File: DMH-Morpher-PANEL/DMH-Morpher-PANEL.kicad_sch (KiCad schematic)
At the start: 4 parts

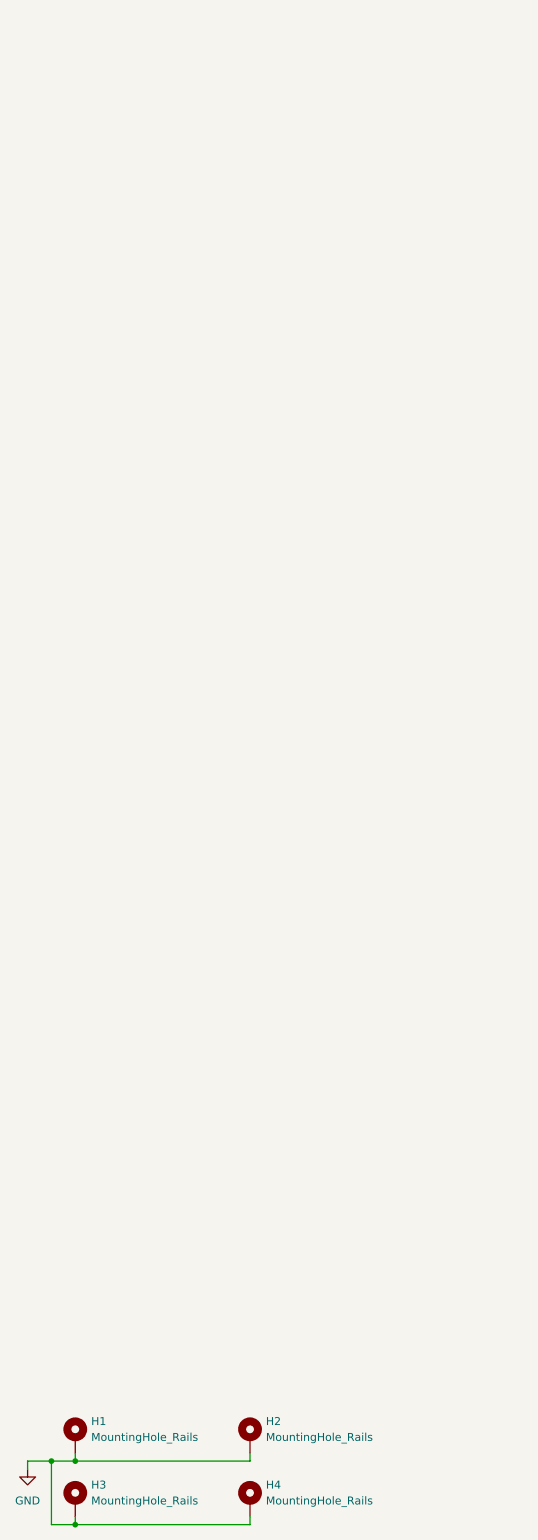
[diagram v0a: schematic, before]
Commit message: Designed panel
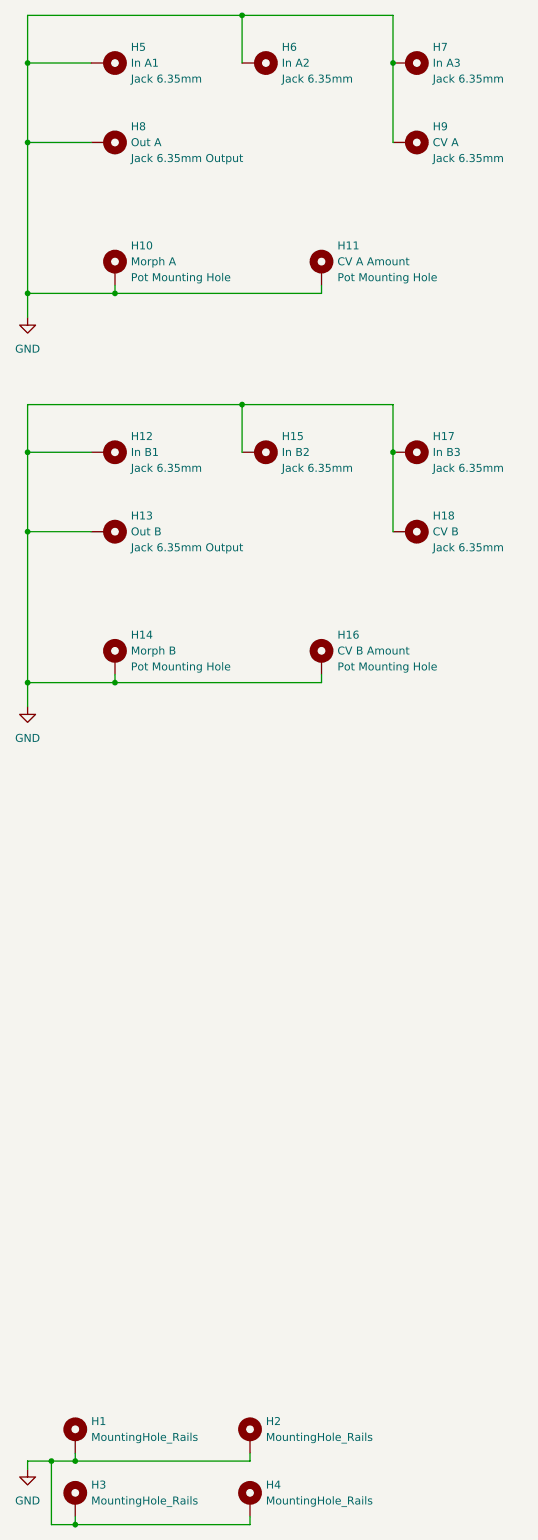
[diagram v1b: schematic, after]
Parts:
- added H10: Morph A, SynthStuff:Pot_Cutout_Medium_v2, symbol SynthStuff:MountingHole_Pot
- added H11: CV A Amount, SynthStuff:Pot_Cutout_Tiny, symbol SynthStuff:MountingHole_Pot
- added H12: In B1, SynthStuff:Jack_6.35mm_Cutout_v3, symbol SynthStuff:MountingHole_Jack6.35mm_v2
- added H13: Out B, SynthStuff:Jack_6.35mm_Cutout_Output_v6, symbol SynthStuff:MountingHole_Jack6.35mm_Output_v2
- added H14: Morph B, SynthStuff:Pot_Cutout_Medium_v2, symbol SynthStuff:MountingHole_Pot
- added H15: In B2, SynthStuff:Jack_6.35mm_Cutout_v3, symbol SynthStuff:MountingHole_Jack6.35mm_v2
- added H16: CV B Amount, SynthStuff:Pot_Cutout_Tiny, symbol SynthStuff:MountingHole_Pot
- added H17: In B3, SynthStuff:Jack_6.35mm_Cutout_v3, symbol SynthStuff:MountingHole_Jack6.35mm_v2
- added H18: CV B, SynthStuff:Jack_6.35mm_Cutout_v3, symbol SynthStuff:MountingHole_Jack6.35mm_v2
- added H5: In A1, SynthStuff:Jack_6.35mm_Cutout_v3, symbol SynthStuff:MountingHole_Jack6.35mm_v2
- added H6: In A2, SynthStuff:Jack_6.35mm_Cutout_v3, symbol SynthStuff:MountingHole_Jack6.35mm_v2
- added H7: In A3, SynthStuff:Jack_6.35mm_Cutout_v3, symbol SynthStuff:MountingHole_Jack6.35mm_v2
- added H8: Out A, SynthStuff:Jack_6.35mm_Cutout_Output_v6, symbol SynthStuff:MountingHole_Jack6.35mm_Output_v2
- added H9: CV A, SynthStuff:Jack_6.35mm_Cutout_v3, symbol SynthStuff:MountingHole_Jack6.35mm_v2
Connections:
- net GND: now also H10.1, H11.1, H12.1, H13.1, H14.1, H15.1, H16.1, H17.1, H18.1, H5.1, H6.1, H7.1, H8.1, H9.1
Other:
- title: Kosmo Format Front Panel - 5 cm -> Morpher
